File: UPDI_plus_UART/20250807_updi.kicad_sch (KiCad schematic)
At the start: 29 parts, among them J1 USB_C_Receptacle_USB2.0_16P, J2 Conn_01x02_Pin, J3 Conn_01x02_Pin, J4 Conn_01x02_Pin, J5 Conn_01x02_Pin, J6 Conn_01x03_Socket, J7 Conn_01x03_Pin, J8 Conn_01x03_Socket, U1 CH342K, U2 AP1117-33

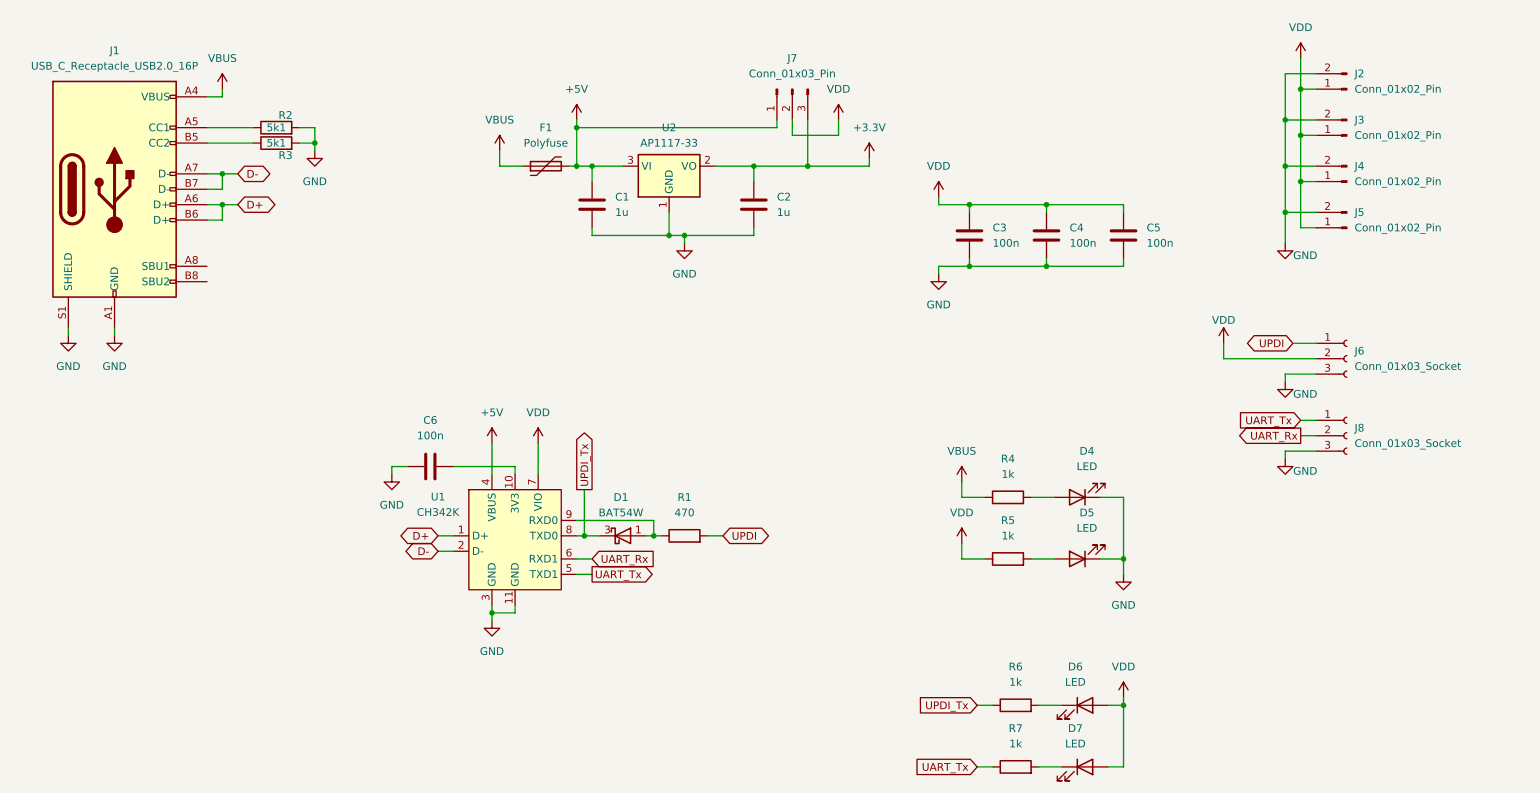
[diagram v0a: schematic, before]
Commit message: Add files via upload
cleaned up schematics and added LCSC part numbers
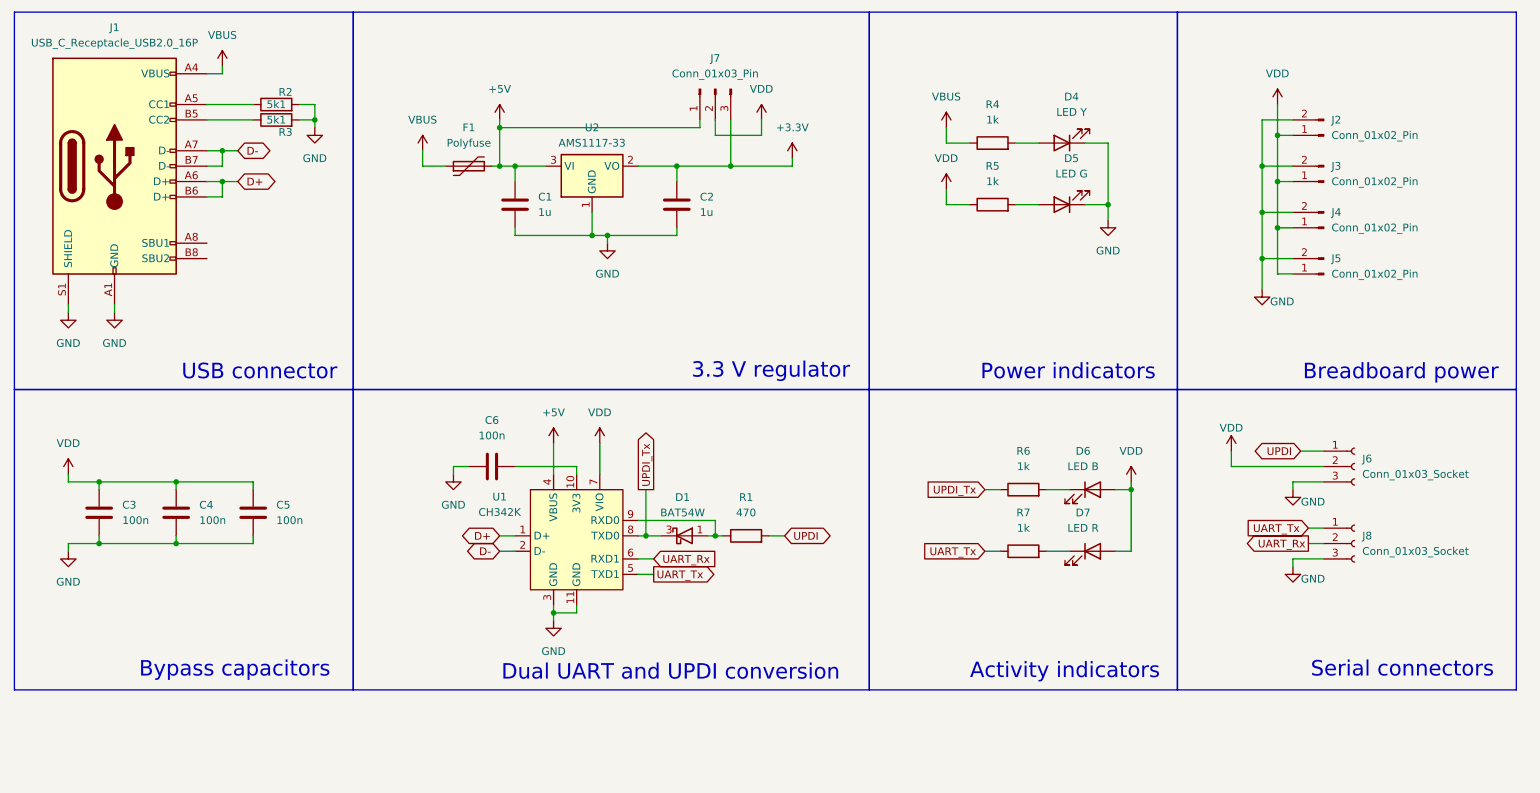
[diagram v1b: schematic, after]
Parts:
- C1, C2: LCSC (none) -> C91186
- C3, C4, C5, C6: LCSC (none) -> C519981
- D1: LCSC (none) -> C41374260
- D4: value LED -> LED Y; LCSC (none) -> C965814
- D5: value LED -> LED G; LCSC (none) -> C84260
- D6: value LED -> LED B; LCSC (none) -> C965817
- D7: value LED -> LED R; LCSC (none) -> C965812
- F1: LCSC (none) -> C883149
- J1: LCSC (none) -> C2765186
- J2, J3, J4, J5: LCSC (none) -> C492401
- J6, J8: LCSC (none) -> C541850
- J7: LCSC (none) -> C41425293
- R1: LCSC (none) -> C5120103
- R2, R3: LCSC (none) -> C2907269
- R4, R5, R6, R7: LCSC (none) -> C6681310
- U1: LCSC (none) -> C2826608
- U2: value AP1117-33 -> AMS1117-33; LCSC (none) -> C426566
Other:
- note added: "3.3 V regulator"
- note added: "Activity indicators"
- note added: "Breadboard power"
- note added: "Bypass capacitors"
- note added: "Dual UART and UPDI conversion"
- note added: "Power indicators"
- note added: "Serial connectors"
- note added: "USB connector"
- title: (none) -> USB UPDI plus UART
- moved on the sheet: C1, C2, C3, C4, C5, C6, D1, D4, D5, D6, D7, F1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
